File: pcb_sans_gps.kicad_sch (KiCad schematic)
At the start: 16 parts, among them J1 Conn_01x20, J2 USB_B_Micro, J3 Conn_01x02, U2 ESP32-C6-MINI-1/U

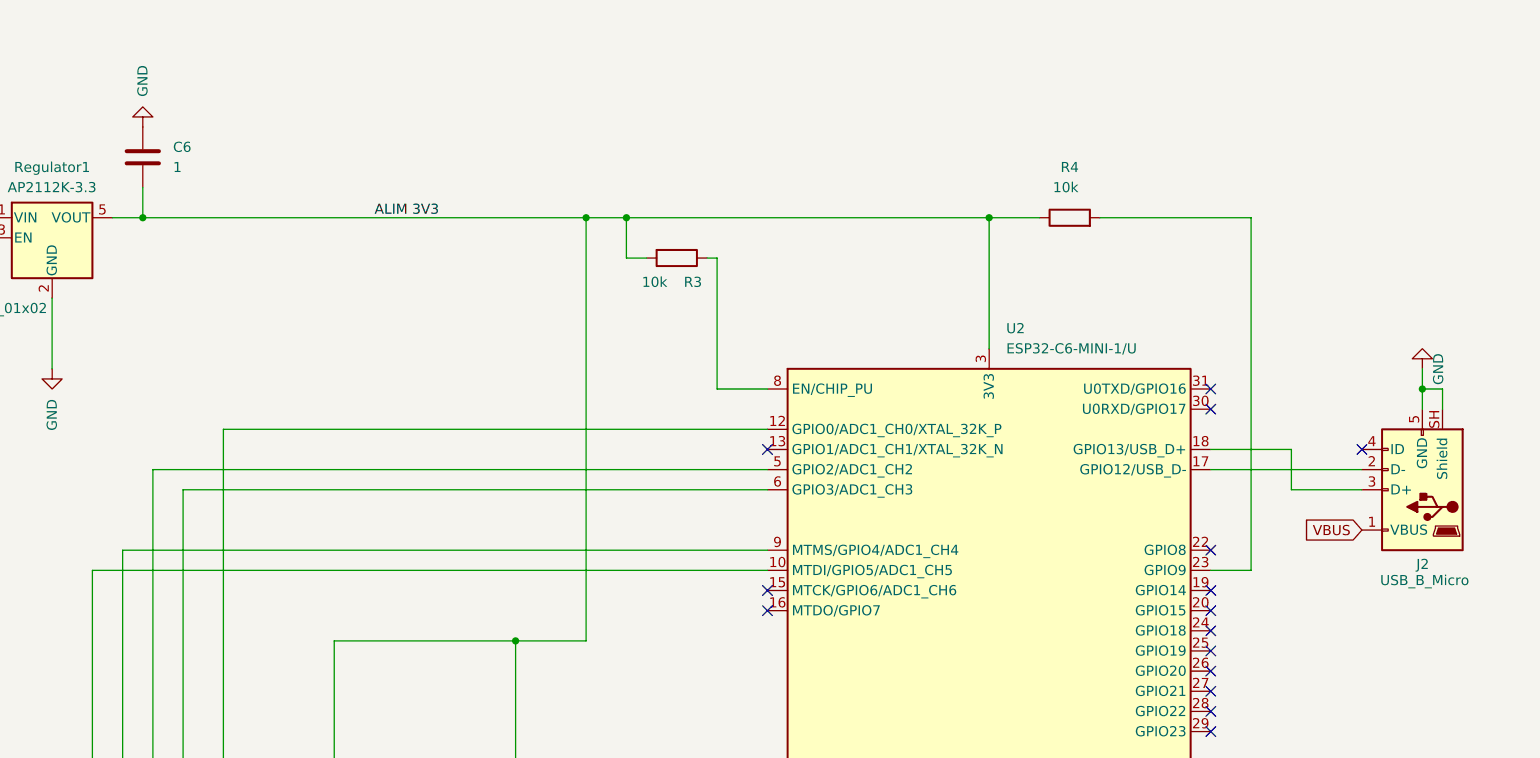
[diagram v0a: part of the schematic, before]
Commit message: Avec connecteur femelle pour GPS
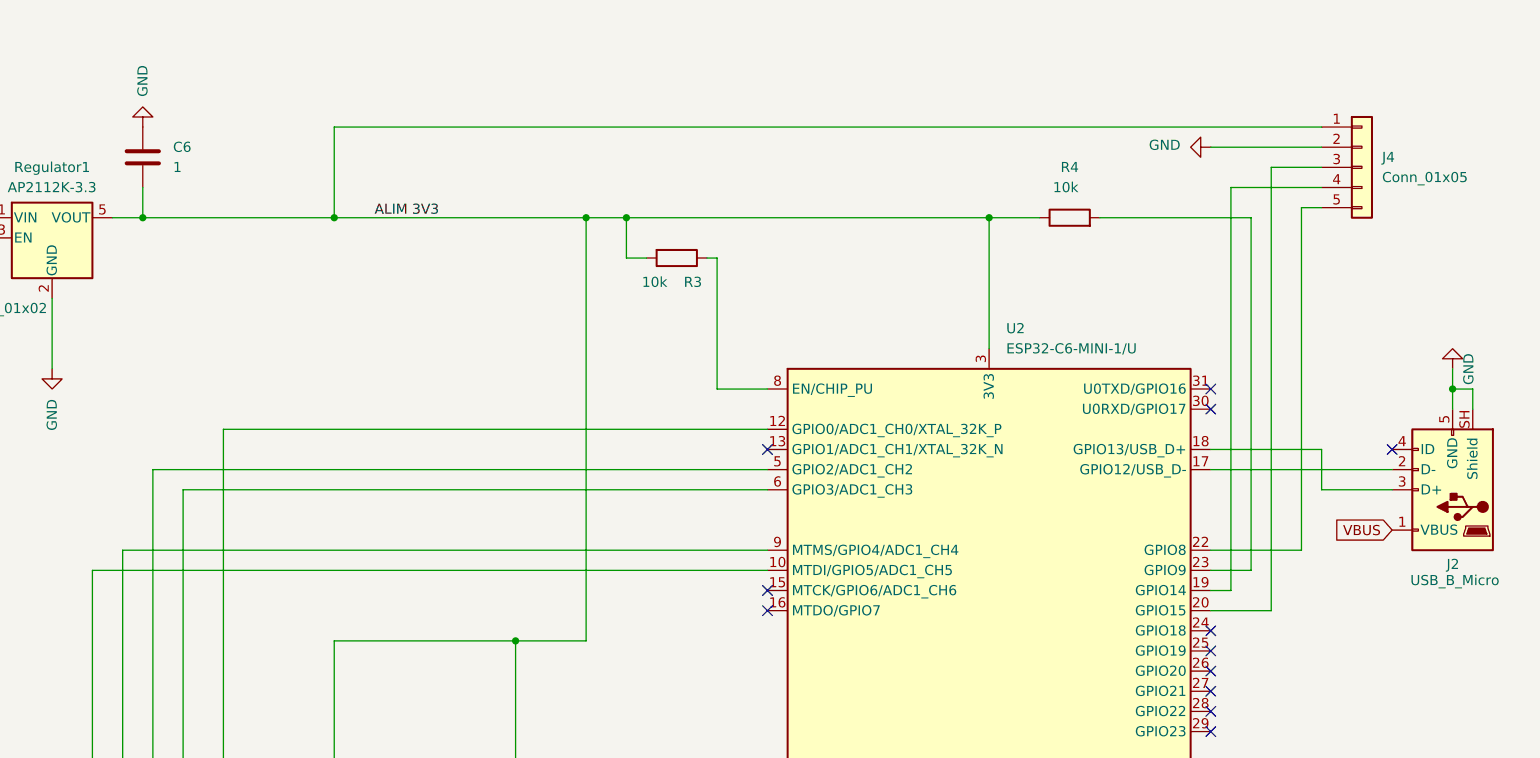
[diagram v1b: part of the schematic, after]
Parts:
- added J4: Conn_01x05, Connector_PinSocket_2.54mm:PinSocket_1x05_P2.54mm_Vertical, symbol Connector_Generic:Conn_01x05
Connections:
- net ALIM 3V3: now also J4.1 (Pin_1)
- net GND: now also J4.2 (Pin_2)
- net at U2.19 (GPIO14): now also J4.4 (Pin_4)
- net at U2.20 (GPIO15): now also J4.3 (Pin_3)
- net at U2.22 (GPIO8): now also J4.5 (Pin_5)
- no-connect marks 17 -> 14
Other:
- moved on the sheet: J2

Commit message: Projet complet - GPS avec Pin Socket et Mounting Holes
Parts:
- added H1, H2, H3, H4: MountingHole, MountingHole:MountingHole_3.2mm_M3, symbol Mechanical:MountingHole
- added TP10, TP15, TP17, TP19, TP20, TP22, TP24, TP4, TP5, TP7, TP8, TP9: TestPoint, TestPoint:TestPoint_Pad_D1.0mm, symbol Connector:TestPoint
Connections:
- net ALIM 3V3: now also TP15.1, TP24.1
- net VBUS: now also TP22.1
- net at J2.2 (D-), U2.17 (GPIO12/USB_D-): now also TP5.1
- net at J2.3 (D+), U2.18 (GPIO13/USB_D+): now also TP4.1
- net at C4.2, C5.2, J3.1 (Pin_1)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: now also TP17.1, TP19.1, TP20.1
- net at MUX1.10 (S0), U2.10 (MTDI/GPIO5/ADC1_CH5): now also TP10.1
- net at MUX1.14 (S2), U2.5 (GPIO2/ADC1_CH2): now also TP7.1
- net at MUX1.13 (S3), U2.6 (GPIO3/ADC1_CH3): now also TP8.1
- net at MUX1.11 (S1), U2.9 (MTMS/GPIO4/ADC1_CH4): now also TP9.1
